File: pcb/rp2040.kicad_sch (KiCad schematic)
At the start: 23 parts, among them SW1 BOOTSEL, U3 W25Q32JVSS, U4 RP2040, Y1 12MHz

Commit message: feat: change flash footprint
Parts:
- U3: value W25Q32JVSS -> W25Q32JVUU; footprint Package_SO:SOIC-8_5.23x5.23mm_P1.27mm -> My_Footprints:USON8 (3x4); LCSC C179173 -> C2999380
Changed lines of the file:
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@@
       (effects (font (size 1.27 1.27)) (justify left))
     )
-    (property "Value" "W25Q32JVSS" (id 1) (at 73.1394 97.8971 0)
+    (property "Value" "W25Q32JVUU" (id 1) (at 73.1394 97.8971 0)
       (effects (font (size 1.27 1.27)) (justify left))
     )
-    (property "Footprint" "Package_SO:SOIC-8_5.23x5.23mm_P1.27mm" (id 2) (at 71.12 106.68 0)
+    (property "Footprint" "My_Footprints:USON8 (3x4)" (id 2) (at 71.12 106.68 0)
       (effects (font (size 1.27 1.27)) hide)
     )
@@
       (effects (font (size 1.27 1.27)) hide)
     )
-    (property "LCSC" "C179173" (id 4) (at 71.12 106.68 0)
+    (property "LCSC" "C2999380" (id 4) (at 71.12 106.68 0)
       (effects (font (size 1.27 1.27)) hide)
     )

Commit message: style: update Titles
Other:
- title: (none) -> Bloop NFC Scanner
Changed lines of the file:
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@@
 (kicad_sch (version 20211123) (generator eeschema)
   (paper "A4")
+  (title_block
+    (title "Bloop NFC Scanner")
+    (date "${DATE}")
+    (rev "${VERSION}")
+  )
   (junction (at 160.02 36.83) (diameter 0) (color 0 0 0 0)
   )

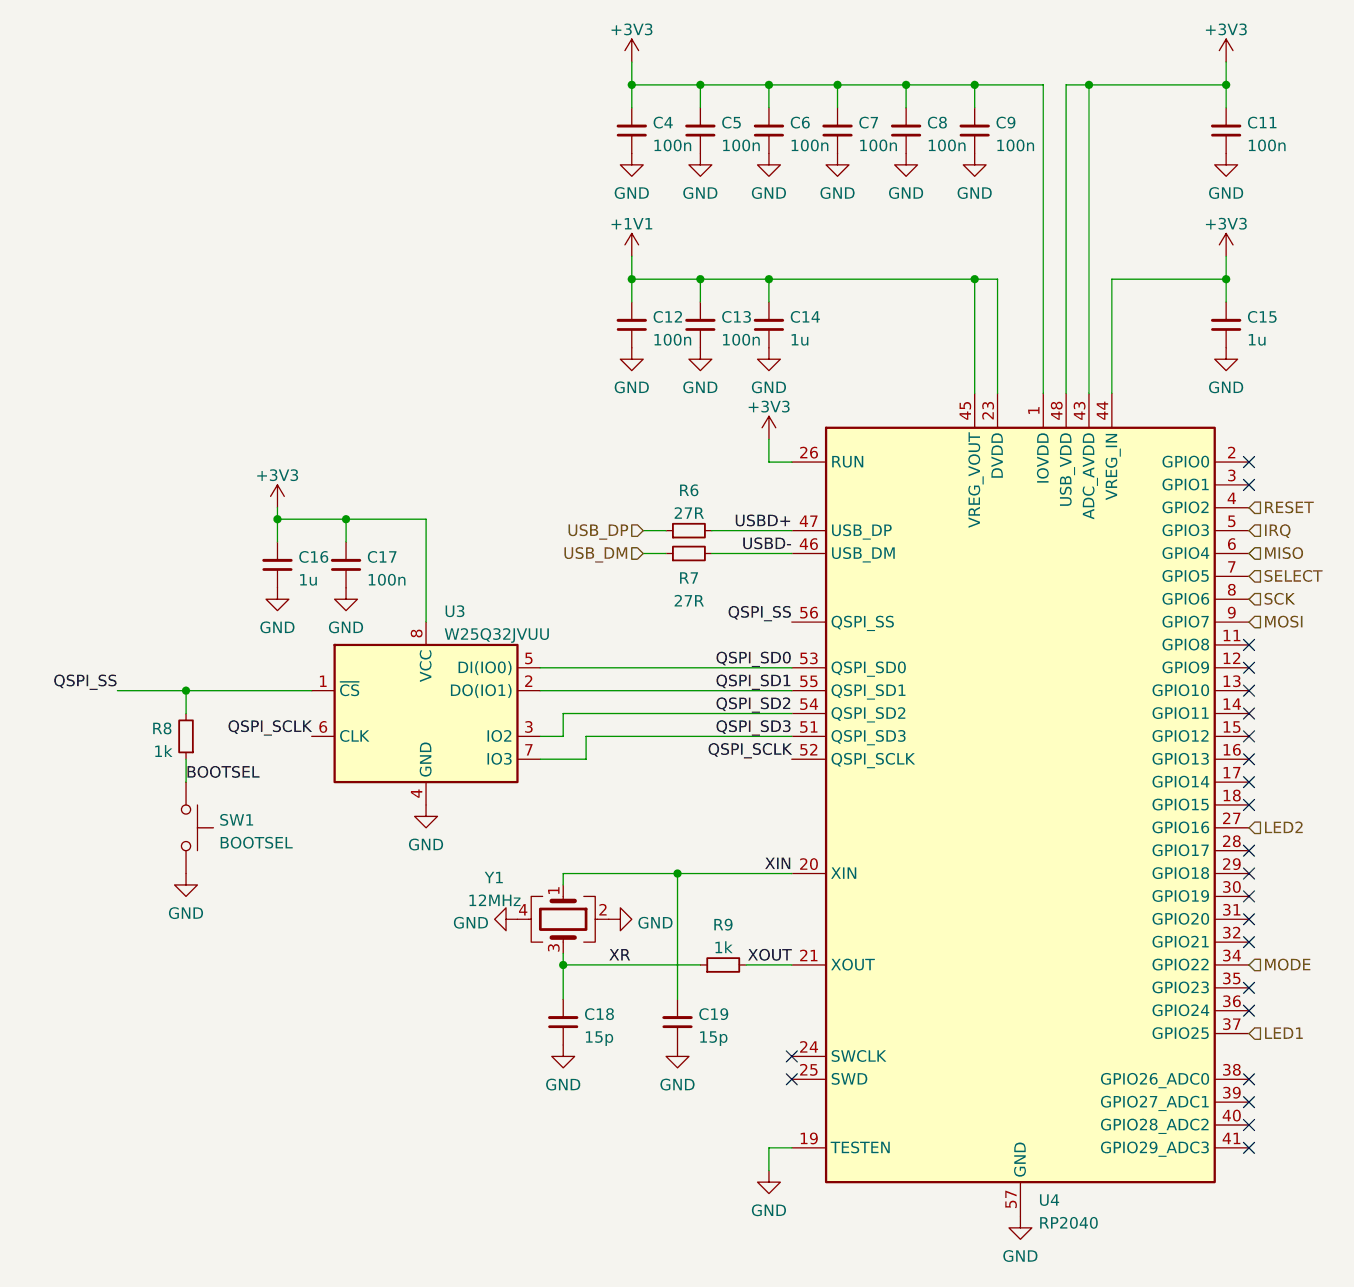
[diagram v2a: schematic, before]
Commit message: fix: change mouse bites position, add silkscreen
This commit includes the switch to KiCad 7 which is why there are so many unrelated changes in the files
The mousebites were moved away from the mode switch
Silkscreen text was added for mode switch and LEDs
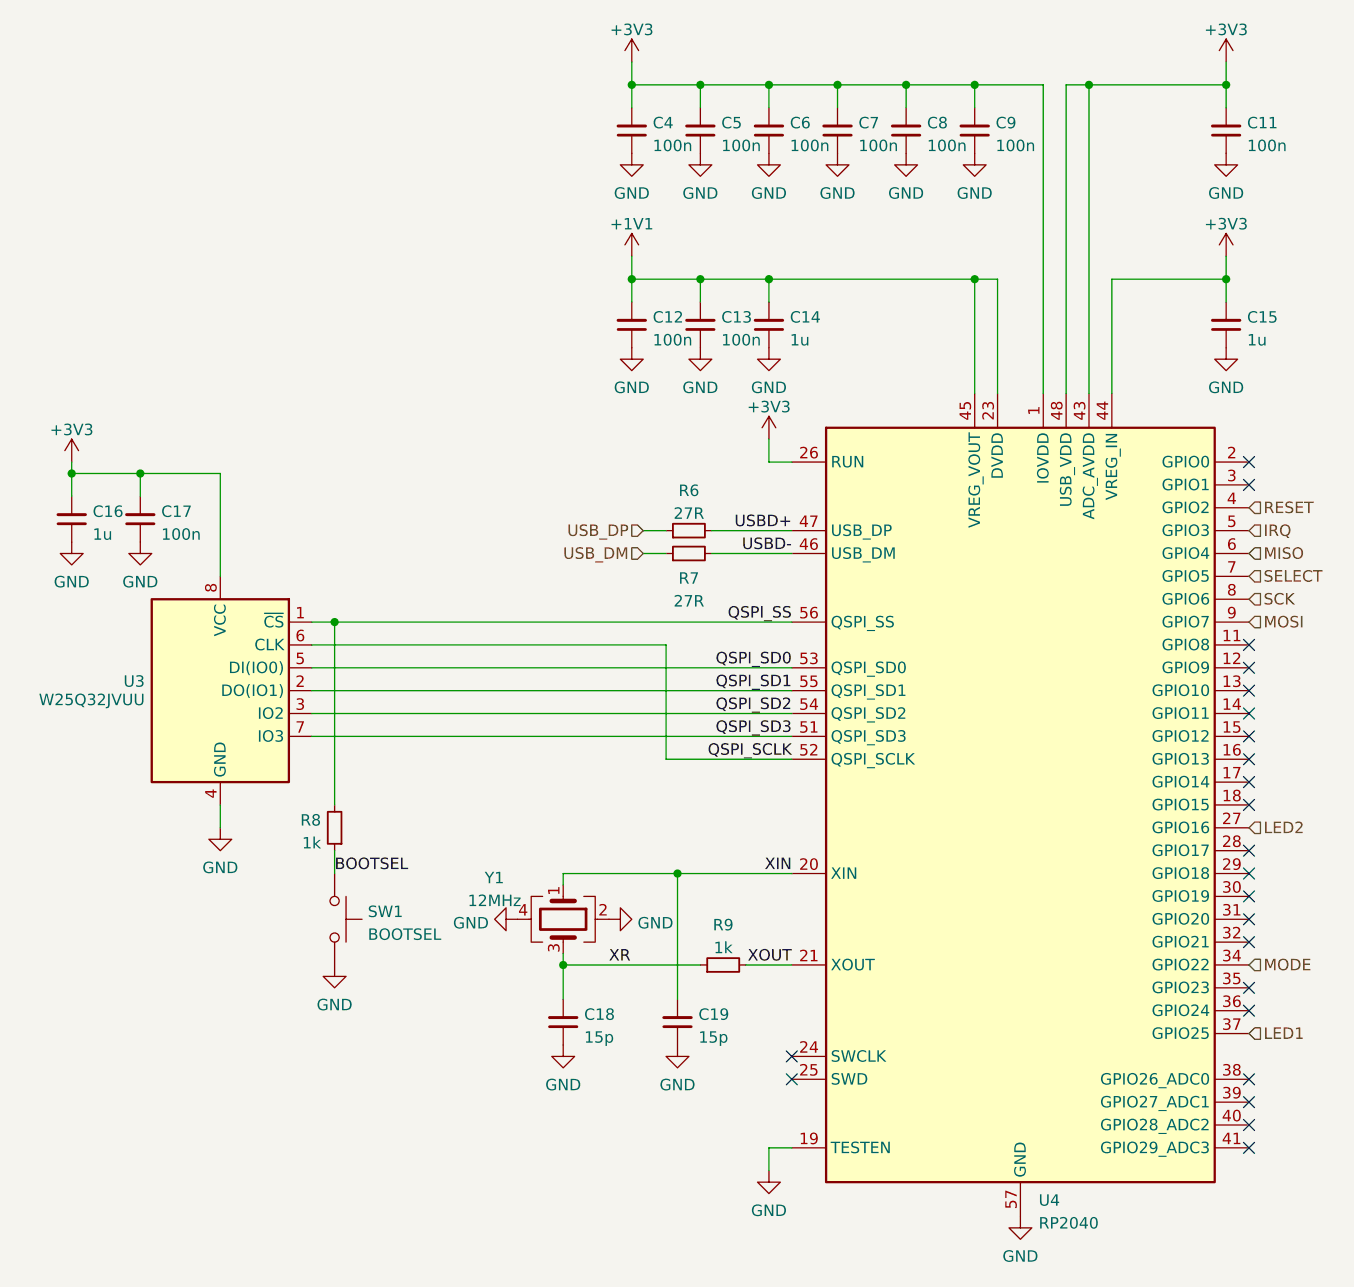
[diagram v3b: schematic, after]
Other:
- moved on the sheet: C16, C17, R8, SW1, U3
